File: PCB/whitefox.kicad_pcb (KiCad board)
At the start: 2 copper layers, 3.6 x 3.2 mm, 12 parts, among them Q1 AO3400A, U1 W25Q128JVS, U2 RP2350B-QFN80, U4 TP4056-42-ESOP8, U5 NCP1117-3.3_SOT223, U6 NCP1117-3.3_SOT223, Y1 Crystal_GND24

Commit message: upload to github
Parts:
- removed U6: NCP1117-3.3_SOT223, Package_TO_SOT_SMD:SOT-223-3_TabPin2
- added C1: 100n, Capacitor_SMD:C_0402_1005Metric, F.Cu at (152.3, 96.7)
- added C10: 100n, Capacitor_SMD:C_0402_1005Metric, F.Cu at (167.9, 93.1)
- added C11: 100n, Capacitor_SMD:C_0402_1005Metric, F.Cu at (156.1, 90.2)
- added C12: 100n, Capacitor_SMD:C_0402_1005Metric, F.Cu at (151.3, 99.2)
- added C13: 100n, Capacitor_SMD:C_0402_1005Metric, F.Cu at (151.2, 108.9)
- added C14: 4.7u, Capacitor_SMD:C_0402_1005Metric, F.Cu at (166.4, 93.0)
- added C15: 4.7u, Capacitor_SMD:C_0402_1005Metric, F.Cu at (165.3, 89.4)
- added C16: 4.7u, Capacitor_SMD:C_0402_1005Metric, F.Cu at (165.8, 91.0)
- added C17: 100n, Capacitor_SMD:C_0402_1005Metric, F.Cu at (155.7, 83.1)
- added C18: 33p, Capacitor_SMD:C_0402_1005Metric, F.Cu at (160.8, 106.5)
- added C19: 33p, Capacitor_SMD:C_0402_1005Metric, F.Cu at (154.7, 108.9)
- added C2: 4.7u, Capacitor_SMD:C_0402_1005Metric, F.Cu at (161.2, 104.0)
- added C20: 10u, Capacitor_SMD:C_0402_1005Metric, F.Cu at (176.2, 72.4)
- added C21: 10u, Capacitor_SMD:C_0402_1005Metric, F.Cu at (173.5, 85.8)
- added C22: 10u, Capacitor_SMD:C_0402_1005Metric, F.Cu at (148.5, 73.2)
- added C23: 10u, Capacitor_SMD:C_0402_1005Metric, F.Cu at (150.5, 73.2)
- added C24: 10u, Capacitor_SMD:C_0402_1005Metric, F.Cu at (160.1, 74.1)
- added C25: 10u, Capacitor_SMD:C_0402_1005Metric, F.Cu at (165.1, 83.0)
- added C3: 100n, Capacitor_SMD:C_0402_1005Metric, F.Cu at (167.3, 96.6)
- added C4: 100n, Capacitor_SMD:C_0402_1005Metric, F.Cu at (160.2, 87.6)
- added C5: 100n, Capacitor_SMD:C_0402_1005Metric, F.Cu at (152.3, 95.7)
- added C6: 100n, Capacitor_SMD:C_0402_1005Metric, F.Cu at (159.2, 105.0)
- added C7: 100n, Capacitor_SMD:C_0402_1005Metric, F.Cu at (156.3, 104.9)
- added C8: 100n, Capacitor_SMD:C_0402_1005Metric, F.Cu at (165.6, 102.5)
- added C9: 100n, Capacitor_SMD:C_0402_1005Metric, F.Cu at (167.3, 97.6)
- added D10: WS2812B-2020, WS2812C-2020:LED_WS2812C-2020, F.Cu at (169.9, 116.0)
- added D11: WS2812B-2020, WS2812C-2020:LED_WS2812C-2020, F.Cu at (172.8, 116.0)
- added D6: WS2812B-2020, WS2812C-2020:LED_WS2812C-2020, F.Cu at (172.8, 112.6)
- added D7: LED, LED_SMD:LED_0603_1608Metric, F.Cu at (164.0, 70.6)
- added D8: 1N5819WS, Diode_SMD:D_SOD-323, F.Cu at (173.9, 72.2)
- added D9: WS2812B-2020, WS2812C-2020:LED_WS2812C-2020, F.Cu at (167.2, 116.0)
- added G***: LOGO, LOGO, B.Cu at (159.9, 89.4)
- added G***: LOGO, LOGO, B.Cu at (159.7, 101.8)
- added G***: LOGO, LOGO, B.Cu at (153.7, 122.1)
- added J1: Micro_SD_Card, TF-01A:TF-01A, F.Cu at (155.8, 118.4)
- added J2: Conn_02x16_Odd_Even, Connector_PinHeader_2.54mm:PinHeader_2x16_P2.54mm_Vertical, F.Cu at (142.0, 75.6)
- added J3: Conn_02x16_Odd_Even, Connector_PinHeader_2.54mm:PinHeader_2x16_P2.54mm_Vertical, F.Cu at (176.4, 75.6)
- added J4: Conn_01x03_MountingPin, Connector_PinHeader_2.54mm:PinHeader_1x03_P2.54mm_Vertical, F.Cu at (167.6, 122.8)
- added J5: USB_C_Receptacle_USB2.0_16P, TYPE-C-31-M-12:TYPE-C-31-M-12, F.Cu at (156.8, 66.6)
- added J6: Conn_01x02, Connector_JST:JST_PH_S2B-PH-K_1x02_P2.00mm_Horizontal, F.Cu at (169.5, 70.2)
- added L1: 3.3u, Inductor_SMD:L_0805_2012Metric, F.Cu at (163.8, 89.6)
- added R1: 1k, Resistor_SMD:R_0402_1005Metric, F.Cu at (171.1, 89.6)
- added R10: 5.1k, Resistor_SMD:R_0402_1005Metric, F.Cu at (155.0, 73.7)
- added R11: 5.1k, Resistor_SMD:R_0402_1005Metric, F.Cu at (171.3, 85.8)
- added R2: 33, Resistor_SMD:R_0402_1005Metric, F.Cu at (166.1, 92.0)
- added R3: 27, Resistor_SMD:R_0402_1005Metric, F.Cu at (160.9, 89.8)
- added R4: 1k, Resistor_SMD:R_0402_1005Metric, F.Cu at (172.1, 97.2)
- added R5: 27, Resistor_SMD:R_0402_1005Metric, F.Cu at (161.9, 89.8)
- added R6: 1k, Resistor_SMD:R_0402_1005Metric, F.Cu at (160.8, 107.5)
- added R7: 1k, Resistor_SMD:R_0402_1005Metric, F.Cu at (172.9, 76.0)
- added R8: 5.1k, Resistor_SMD:R_0402_1005Metric, F.Cu at (158.3, 73.9)
- added R9: 10k, Resistor_SMD:R_0402_1005Metric, F.Cu at (167.6, 72.8)
- added REF**: MountingHole_2.2mm_M2, MountingHole:MountingHole_2.2mm_M2, F.Cu at (177.9, 68.0)
- added REF**: MountingHole_2.2mm_M2, MountingHole:MountingHole_2.2mm_M2, F.Cu at (142.9, 123.6)
- added REF**: MountingHole_2.2mm_M2, MountingHole:MountingHole_2.2mm_M2, F.Cu at (177.9, 123.6)
- added REF**: MountingHole_2.2mm_M2, MountingHole:MountingHole_2.2mm_M2, F.Cu at (142.9, 68.0)
- added SW1: SW_Push, TS-1088-TS-1088-ARXXX:TS-1088-ARXXX, F.Cu at (172.1, 93.1)
- added SW2: SW_Push, TS-1088-TS-1088-ARXXX:TS-1088-ARXXX, F.Cu at (172.1, 100.7)
- added U3: AMS1117-3.3, Package_TO_SOT_SMD:SOT-223-3_TabPin2, F.Cu at (150.6, 78.2)
- D1, D2, D3, D4: value SK6812MINI-E -> WS2812B-2020; footprint LED_SMD:LED_SK6812MINI-E_3.2x2.8mm_P1.5mm_ReverseMount -> WS2812C-2020:LED_WS2812C-2020
- D5: value 1N5819WS -> WS2812B-2020; footprint Diode_SMD:D_SOD-323 -> WS2812C-2020:LED_WS2812C-2020
- Q1: value AO3400A -> AO3401A
- U5: value NCP1117-3.3_SOT223 -> AMS1117-3.3
- moved D1 81.7 mm to (167.2, 109.2), turned to 90 degrees
- moved D2 79.3 mm to (169.9, 109.2), turned to 90 degrees
- moved D3 77.3 mm to (172.8, 109.2), turned to 90 degrees
- moved D4 72.6 mm to (167.2, 112.6), turned to 90 degrees
- moved D5 59.8 mm to (169.9, 112.6), turned to 90 degrees
- moved Y1 53.8 mm to (157.8, 107.7), turned to -90 degrees
- moved U5 52.1 mm to (164.8, 77.8), turned to -90 degrees
- moved U4 43.8 mm to (171.1, 80.5), turned to 90 degrees
- moved U1 41.6 mm to (151.7, 86.1)
- moved U2 28.6 mm to (159.8, 97.3)
- moved Q1 14.9 mm to (170.8, 74.2)
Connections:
- D1 pad 1: GND -> Net-(D1-DOUT)
- D1 pad 2: NEOPIXEL -> GND
- D1 pad 3: +3V3 -> NEOPIXEL
- D1 pad 4: Net-(D1-DOUT) -> VBUS
- D2 pad 1: GND -> Net-(D2-DOUT)
- D2 pad 2: Net-(D1-DOUT) -> GND
- D2 pad 3: +3V3 -> Net-(D1-DOUT)
- D2 pad 4: Net-(D2-DOUT) -> VBUS
- D3 pad 1: GND -> Net-(D3-DOUT)
- D3 pad 2: Net-(D2-DOUT) -> GND
- D3 pad 3: +3V3 -> Net-(D2-DOUT)
- D3 pad 4: Net-(D3-DOUT) -> VBUS
- D4 pad 1: GND -> Net-(D4-DOUT)
- D4 pad 2: Net-(D3-DOUT) -> GND
- D4 pad 3: +3V3 -> Net-(D3-DOUT)
- D4 pad 4: unconnected-(D4-DOUT-Pad4) -> VBUS
- D5 pad 1: MOSFET_OUT -> Net-(D5-DOUT)
- D5 pad 2: VBUS -> GND
- U2 pad 1: I2C0_SDA -> GPIO4
- U2 pad 11: UART0_TX -> GPIO12
- U2 pad 12: UART0_RX -> GPIO13
- U2 pad 13: UART0_CTS -> GPIO14
- U2 pad 14: UART0_RTS -> GPIO15
- U2 pad 16: NEOPIXEL -> GPIO16
- U2 pad 2: I2C0_SCL -> GPIO5
- U2 pad 20: UART1_TX -> GPIO20
- U2 pad 21: UART1_RX -> GPIO21
- U2 pad 22: UART1_CTS -> GPIO22
- U2 pad 23: UART1_RTS -> GPIO23
- U2 pad 25: GPIO24 -> SPI1_RX_SD_MISO
- U2 pad 26: GPIO25 -> SPI1_CSN_SD_CS
- U2 pad 27: GPIO26 -> SPI1_SCK_SD_SCK
- U2 pad 28: GPIO27 -> SPI1_TX_SD_MOSI
- U2 pad 3: I2C1_SDA -> GPIO6
- U2 pad 36: SPI1_RX_SD_MISO -> GPIO28
- U2 pad 37: SPI1_CSN_SD_CS -> GPIO29
- U2 pad 38: SPI1_SCK_SD_SCK -> GPIO30
- U2 pad 39: SPI1_TX_SD_MOSI -> GPIO31
- U2 pad 4: I2C1_SCL -> GPIO7
- U2 pad 48: GPIO39 -> NEOPIXEL
- U2 pad 6: GPIO08 -> GPIO8
- U2 pad 7: GPIO09 -> GPIO9
- U2 pad 77: SPI0_RX -> GPIO0
- U2 pad 78: SPI0_CSN -> GPIO1
- U2 pad 79: SPI0_SCK -> GPIO2
- U2 pad 80: SPI0_TX -> GPIO3
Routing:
- net VBUS: track 0.00 -> 159.8 mm, vias 0 -> 10
- net GND: track 0.00 -> 146.7 mm, vias 0 -> 92
- net +3V3: track 0.00 -> 75.5 mm, vias 0 -> 17
- net +1V1: track 0.00 -> 48.7 mm
- net QSPI_SS: track 0.00 -> 44.3 mm, vias 0 -> 2
- net SWCLK: track 0.00 -> 44.1 mm, vias 0 -> 1
- net NEOPIXEL: track 0.00 -> 43.9 mm, vias 0 -> 2
- net SWDIO: track 0.00 -> 39.4 mm, vias 0 -> 1
- net GPIO22: track 0.00 -> 37.1 mm, vias 0 -> 1
- net GPIO44: track 0.00 -> 24.3 mm
- net GPIO1: track 0.00 -> 23.6 mm, vias 0 -> 1
- net GPIO23: track 0.00 -> 22.9 mm, vias 0 -> 2
- net DATA-: track 0.00 -> 22.4 mm
- net DATA+: track 0.00 -> 22.4 mm
- net GPIO46: track 0.00 -> 22.0 mm
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- added copper zone on In2.Cu, net +3V3
- added copper zone on B.Cu, net GND
- added copper zone on F.Cu, net GND
- added copper zone on In1.Cu, net GND
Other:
- board size 3.6 x 3.2 mm -> 41 x 61.6 mm
- copper layers 2 -> 4
- board text added: "#bonkthesoup"
- board text added: "0 1"
- board text added: "1 2 3 4 5 6 7 8 9"
- board text added: "10 11"
- board text added: "12 13"
- board text added: "14 15"
- board text added: "16 17"
- board text added: "18 19"
- board text added: "2 3"
- board text added: "20 21"
- board text added: "22 RUN"
- board text added: "28 23"
- board text added: "30 29"
- board text added: "32 31"
- board text added: "34 33"
- board text added: "36 35"
- board text added: "38 37"
- board text added: "3v3"
- board text added: "4 5"
- board text added: "40 41"
- board text added: "42 43"
- board text added: "44 45"
- board text added: "46 47"
- board text added: "6 7"
- board text added: "8 9"
- board text added: "BATT"
- board text added: "GND"
- board text added: "GND VBUS"
- board text added: "NEOPX"
- board text added: "RP2350B"
- board text added: "RP350B"
- board text added: "SIG GND PWR SIG"
- board text added: "SWCLK GND SWDIO"
- board text added: "SWDIO SWCLK"
- board text added: "USB"
- board text added: "VBUS"
- board text added: "made by a human"
- board text added: "made by ritam <3"
- board text added: "microSD"
- board text added: "ouch."
- board text added: "white fox v1"

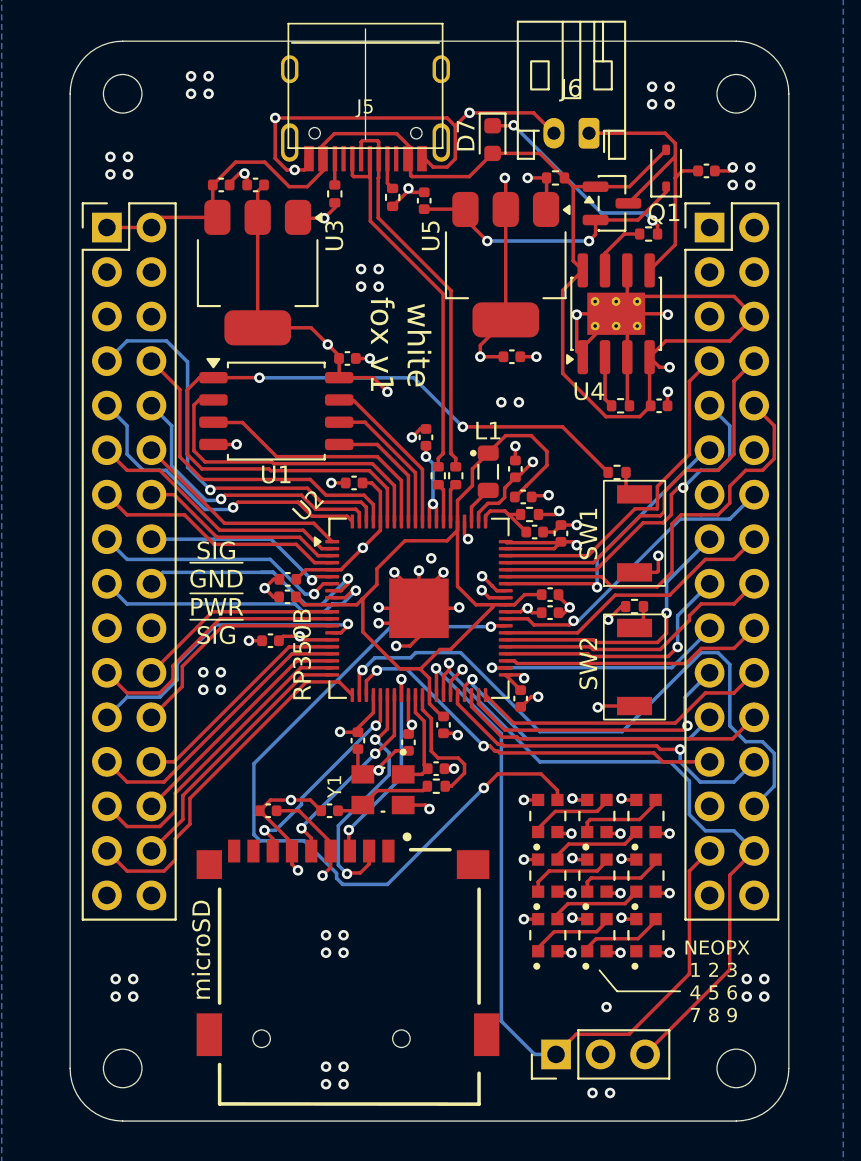
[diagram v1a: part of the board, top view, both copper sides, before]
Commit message: add decoupling caps
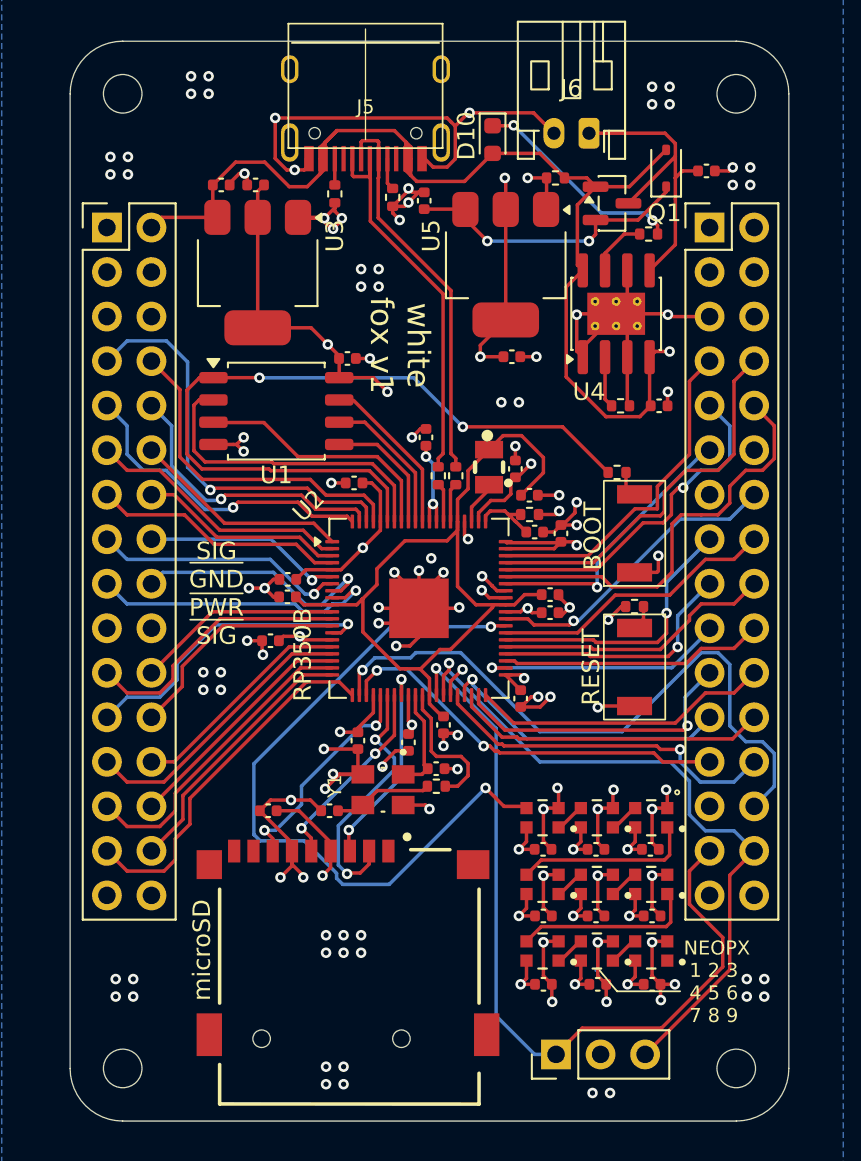
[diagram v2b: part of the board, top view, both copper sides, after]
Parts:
- added C20: 100n, Capacitor_SMD:C_0402_1005Metric, F.Cu at (166.9, 111.1)
- added C21: 100n, Capacitor_SMD:C_0402_1005Metric, F.Cu at (169.9, 111.1)
- added C22: 100n, Capacitor_SMD:C_0402_1005Metric, F.Cu at (173.0, 111.1)
- added C23: 100n, Capacitor_SMD:C_0402_1005Metric, F.Cu at (166.9, 114.9)
- added C24: 100n, Capacitor_SMD:C_0402_1005Metric, F.Cu at (169.9, 114.9)
- added C25: 100n, Capacitor_SMD:C_0402_1005Metric, F.Cu at (173.1, 114.9)
- added C26: 100n, Capacitor_SMD:C_0402_1005Metric, F.Cu at (166.9, 118.8)
- added C27: 100n, Capacitor_SMD:C_0402_1005Metric, F.Cu at (170.0, 118.8)
- added C28: 100n, Capacitor_SMD:C_0402_1005Metric, F.Cu at (173.1, 118.8)
- L1: footprint Inductor_SMD:L_0805_2012Metric -> jlc_kicad_footprint:IND-SMD_L2.0-W1.6_AOTA-B201610S3R3-101-T
- moved D7 0.95 mm to (166.8, 116.9), turned to 180 degrees
- moved D9 0.95 mm to (173.1, 116.9), turned to 180 degrees
- moved D8 0.90 mm to (169.9, 116.9), turned to 180 degrees
- moved D4 0.58 mm to (166.8, 113.1), turned to 180 degrees
- moved D6 0.58 mm to (173.1, 113.1), turned to 180 degrees
- moved D5 0.50 mm to (169.9, 113.1), turned to 180 degrees
- moved C16 0.36 mm to (166.1, 90.9)
- moved D1 0.32 mm to (166.8, 109.3), turned to 180 degrees
- moved D3 0.32 mm to (173.1, 109.3), turned to 180 degrees
- moved L1 0.27 mm to (163.8, 89.3)
- moved D2 0.10 mm to (169.9, 109.3), turned to 180 degrees
- renumbered C18 to C17, C17 to C18, C20 to C29, C21 to C30, C22 to C31, C23 to C32, C24 to C33, C25 to C34, D7 to D10, D8 to D11, D9 to D7, D10 to D8, D11 to D9
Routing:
- net GND: track 146.7 -> 190.6 mm, vias 92 -> 114
- net Net-(D6-DOUT): track 5.34 -> 10.4 mm
- net Net-(D3-DOUT): track 5.31 -> 10.3 mm
- net Net-(D2-DOUT): track 5.10 -> 1.73 mm
- net Net-(D5-DOUT): track 5.10 -> 1.73 mm
- net Net-(D4-DOUT): track 5.05 -> 1.73 mm
- net Net-(D7-DOUT): track 4.86 -> 1.73 mm
- net Net-(D8-DOUT): track 4.84 -> 1.73 mm
- net Net-(D1-DOUT): track 4.84 -> 1.73 mm
- net NEOPIXEL: track 43.9 -> 41.3 mm
- net SWCLK: track 44.1 -> 46.6 mm
- net VBUS: track 159.8 -> 160.7 mm
- net GPIO10: track 14.9 -> 14.2 mm
- net +1V1: track 48.7 -> 48.0 mm
- net XOUT: track 7.53 -> 8.05 mm
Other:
- board text added: "BOOT"
- board text added: "RESET"
